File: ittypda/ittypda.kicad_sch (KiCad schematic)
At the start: 149 parts, among them CN1 S2B-PH-SM4-TB, J1 USB_C_Receptacle_USB2.0_14P, J2 Conn_01x04_Pin, SW1 Switch, SW10 Switch, SW11 Switch, SW12 Switch, SW13 Switch, SW14 Switch, SW15 Switch, SW16 Switch, SW17 Switch, SW18 Switch, SW19 Switch, SW2 Switch, SW20 Switch, SW21 Switch, SW22 Switch, SW23 Switch, SW24 Switch, SW25 SLIDE SWITCH, SW26 Switch, SW27 Switch, SW28 Switch, SW29 Switch, SW3 Switch, SW30 Switch, SW31 Switch, SW32 Switch, SW33 Switch, SW34 Switch, SW36 Switch, SW37 Switch, SW38 Switch, SW39 Switch, SW4 Switch, SW41 Switch, SW42 Switch, SW43 Switch, SW44 Switch, SW45 Switch, SW46 Switch, SW47 Switch, SW48 Switch, SW49 Switch, SW5 Switch, SW50 Switch, SW51 Switch, SW52 Switch, SW53 Switch, SW54 Switch, SW55 Switch, SW56 Switch, SW57 Switch, SW58 Switch, SW59 Switch, SW6 Switch, SW60 Switch, SW62 SW_SPDT, SW7 Switch, SW8 Switch, SW9 Switch, U1 STM32F401RETx, U2 BQ24040DSQR, U3 TLV75801PDRV, Y1 16Mhz

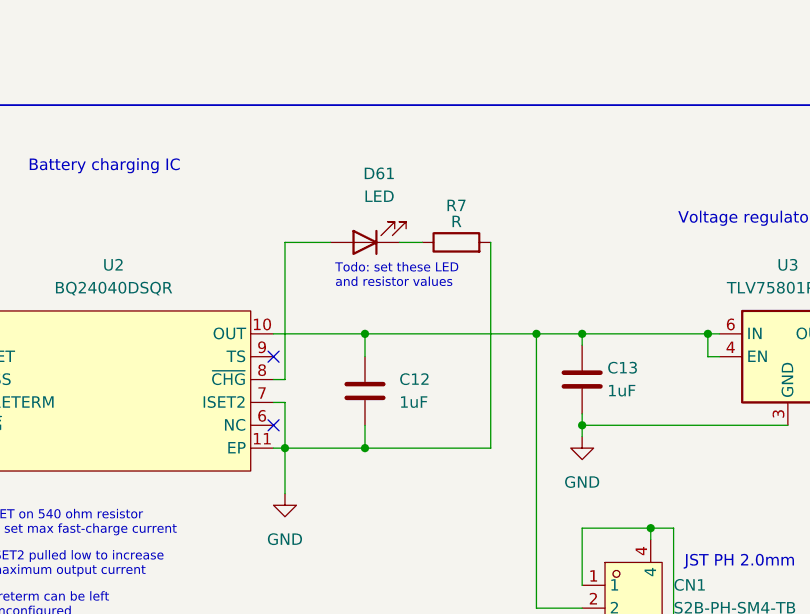
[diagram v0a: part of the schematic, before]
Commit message: add values and footprint for charging status LED
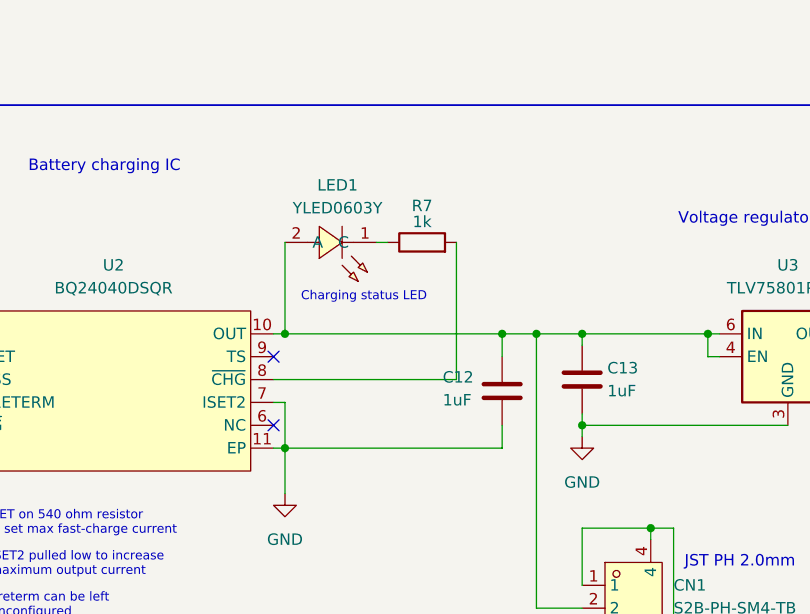
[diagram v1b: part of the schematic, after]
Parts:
- removed D61: LED, symbol Device:LED
- added LED1: YLED0603Y, easyeda2kicad:LED0603-RD-1, symbol easyeda2kicad:YLED0603Y
- R7: value R -> 1k
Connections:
- net GND: no longer R7.2
- net at C12.1, C13.1, CN1.2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: now also LED1.2 (A)
- net at R7.1: now also LED1.1 (C)
- net at U2.8 (~{CHG}): now also R7.2
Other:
- note added: "Charging status LED"
- note removed: "Todo: set these LED and resistor values"
- moved on the sheet: C12, R7
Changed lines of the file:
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@@
 		)
 	)
-	(text "Todo: set these LED\nand resistor values"
+	(text "Charging status LED"
 		(exclude_from_sim no)
-		(at 150.368 171.45 0)
+		(at 146.558 173.736 0)
 		(effects
 			(font
@@
 	)
 	(junction
+		(at 144.78 177.8)
+		(diameter 0)
+		(color 0 0 0 0)
+	)
+	(junction
 		(at 36.83 45.72)
 		(diameter 0)
@@
 	)
 	(junction
-		(at 153.67 177.8)
-		(diameter 0)
-		(color 0 0 0 0)
-	)
-	(junction
 		(at 104.14 118.11)
 		(diameter 0)
@@
 	)
 	(junction
-		(at 153.67 190.5)
-		(diameter 0)
-		(color 0 0 0 0)
-	)
-	(junction
 		(at 209.55 173.99)
 		(diameter 0)
@@
 	)
 	(junction
+		(at 168.91 177.8)
+		(diameter 0)
+		(color 0 0 0 0)
+	)
+	(junction
 		(at 62.23 60.96)
 		(diameter 0)
@@
 	(wire
 		(pts
-			(xy 153.67 177.8) (xy 172.72 177.8)
+			(xy 168.91 177.8) (xy 172.72 177.8)
 		)
 		(stroke
@@
 	(wire
 		(pts
-			(xy 153.67 190.5) (xy 144.78 190.5)
+			(xy 168.91 190.5) (xy 144.78 190.5)
 		)
 		(stroke
@@
 	(wire
 		(pts
+			(xy 144.78 177.8) (xy 168.91 177.8)
+		)
+		(stroke
+			(width 0)
+			(type default)
+		)
+	)
+	(wire
+		(pts
 			(xy 76.2 137.16) (xy 90.17 137.16)
 		)
@@
 	(wire
 		(pts
-			(xy 153.67 187.96) (xy 153.67 190.5)
+			(xy 168.91 187.96) (xy 168.91 190.5)
 		)
 		(stroke
@@
 	(wire
 		(pts
-			(xy 153.67 177.8) (xy 153.67 180.34)
+			(xy 168.91 177.8) (xy 168.91 180.34)
 		)
 		(stroke
@@
 	(wire
 		(pts
-			(xy 144.78 167.64) (xy 149.86 167.64)
-		)
-		(stroke
-			(width 0)
-			(type default)
-		)
-	)
-	(wire
-		(pts
 			(xy 312.42 76.2) (xy 314.96 76.2)
 		)
@@
 	(wire
 		(pts
-			(xy 144.78 182.88) (xy 144.78 167.64)
-		)
-		(stroke
-			(width 0)
-			(type default)
-		)
-	)
-	(wire
-		(pts
 			(xy 62.23 60.96) (xy 76.2 60.96)
 		)
@@
 	(wire
 		(pts
-			(xy 143.51 182.88) (xy 144.78 182.88)
+			(xy 143.51 182.88) (xy 163.83 182.88)
 		)
 		(stroke
@@
 	(wire
 		(pts
-			(xy 157.48 167.64) (xy 160.02 167.64)
+			(xy 154.94 167.64) (xy 156.21 167.64)
 		)
 		(stroke
@@
 	(wire
 		(pts
-			(xy 143.51 177.8) (xy 153.67 177.8)
+			(xy 143.51 177.8) (xy 144.78 177.8)
 		)
 		(stroke
@@
 	(wire
 		(pts
+			(xy 163.83 167.64) (xy 163.83 182.88)
+		)
+		(stroke
+			(width 0)
+			(type default)
+		)
+	)
+	(wire
+		(pts
 			(xy 67.31 177.8) (xy 67.31 176.53)
 		)
@@
 	(wire
 		(pts
-			(xy 153.67 190.5) (xy 167.64 190.5)
-		)
-		(stroke
-			(width 0)
-			(type default)
-		)
-	)
-	(wire
-		(pts
 			(xy 120.65 64.77) (xy 121.92 64.77)
 		)
@@
 	(wire
 		(pts
-			(xy 167.64 190.5) (xy 167.64 167.64)
-		)
-		(stroke
-			(width 0)
-			(type default)
-		)
-	)
-	(wire
-		(pts
 			(xy 64.77 64.77) (xy 64.77 83.82)
 		)
@@
 	(wire
 		(pts
+			(xy 144.78 167.64) (xy 144.78 177.8)
+		)
+		(stroke
+			(width 0)
+			(type default)
+		)
+	)
+	(wire
+		(pts
 			(xy 162.56 83.82) (xy 163.83 83.82)
 		)
@@
 	(symbol
 		(lib_id "Device:R")
-		(at 163.83 167.64 90)
+		(at 160.02 167.64 90)
 		(unit 1)
 		(body_style 1)
@@
 		(dnp no)
 		(property "Reference" "R7"
-			(at 163.83 163.576 90)
+			(at 160.02 163.576 90)
 			(show_name no)
 			(do_not_autoplace no)
@@
 			)
 		)
-		(property "Value" "R"
-			(at 163.83 165.354 90)
+		(property "Value" "1k"
+			(at 160.02 165.354 90)
 			(show_name no)
 			(do_not_autoplace no)
@@
 		)
 		(property "Footprint" ""
-			(at 163.83 169.418 90)
+			(at 160.02 169.418 90)
 			(hide yes)
 			(show_name no)
@@
 		)
 		(property "Datasheet" ""
-			(at 163.83 167.64 0)
+			(at 160.02 167.64 0)
 			(hide yes)
 			(show_name no)
@@
 		)
 		(property "Description" "Resistor"
-			(at 163.83 167.64 0)
+			(at 160.02 167.64 0)
 			(hide yes)
 			(show_name no)
@@
 	)
 	(symbol
-		(lib_id "Device:LED")
-		(at 153.67 167.64 180)
+		(lib_id "power:GND")
+		(at 144.78 195.58 0)
 		(unit 1)
 		(body_style 1)
@@
 		(dnp no)
 		(fields_autoplaced yes)
-		(property "Reference" "D61"
-			(at 155.2575 160.02 0)
+		(property "Reference" "#PWR017"
+			(at 144.78 201.93 0)
+			(hide yes)
 			(show_name no)
 			(do_not_autoplace no)
@@
 			)
 		)
-		(property "Value" "LED"
-			(at 155.2575 162.56 0)
+		(property "Value" "GND"
+			(at 144.78 200.66 0)
 			(show_name no)
 			(do_not_autoplace no)
@@
 		)
 		(property "Footprint" ""
-			(at 153.67 167.64 0)
+			(at 144.78 195.58 0)
 			(hide yes)
 			(show_name no)
@@
 		)
 		(property "Datasheet" ""
-			(at 153.67 167.64 0)
-			(hide yes)
-			(show_name no)
-			(do_not_autoplace no)
-			(effects
-				(font
-					(size 1.27 1.27)
-				)
-			)
-		)
-		(property "Description" "Light emitting diode"
-			(at 153.67 167.64 0)
+			(at 144.78 195.58 0)
 			(hide yes)
 			(show_name no)
@@
 			)
 		)
-		(property "Sim.Pins" "1=K 2=A"
-			(at 153.67 167.64 0)
+		(property "Description" "Power symbol creates a global label with name \"GND\" , ground"
+			(at 144.78 195.58 0)
 			(hide yes)
 			(show_name no)
@@
 			)
 		)
-		(pin "2"
-		)
 		(pin "1"
 		)
@@
 			(project "ittypda"
 				(path "/d1aa8f6c-1644-4347-b86d-2b771500f753"
-					(reference "D61")
+					(reference "#PWR017")
 					(unit 1)
 				)
@@
 	)
 	(symbol
-		(lib_id "power:GND")
-		(at 144.78 195.58 0)
+		(lib_id "easyeda2kicad:YLED0603Y")
+		(at 149.86 168.91 180)
 		(unit 1)
 		(body_style 1)
@@
 		(dnp no)
 		(fields_autoplaced yes)
-		(property "Reference" "#PWR017"
-			(at 144.78 201.93 0)
+		(property "Reference" "LED1"
+			(at 150.62 161.29 0)
+			(show_name no)
+			(do_not_autoplace no)
+			(effects
+				(font
+					(size 1.27 1.27)
+				)
+			)
+		)
+		(property "Value" "YLED0603Y"
+			(at 150.62 163.83 0)
+			(show_name no)
+			(do_not_autoplace no)
+			(effects
+				(font
+					(size 1.27 1.27)
+				)
+			)
+		)
+		(property "Footprint" "easyeda2kicad:LED0603-RD-1"
+			(at 149.86 160.02 0)
 			(hide yes)
 			(show_name no)
@@
 			)
 		)
-		(property "Value" "GND"
-			(at 144.78 200.66 0)
+		(property "Datasheet" "https://www.lcsc.com/datasheet/C19273152.pdf"
+			(at 149.86 157.48 0)
+			(hide yes)
 			(show_name no)
 			(do_not_autoplace no)
@@
 			)
 		)
-		(property "Footprint" ""
-			(at 144.78 195.58 0)
+		(property "Description" ""
+			(at 149.86 168.91 0)
 			(hide yes)
 			(show_name no)
@@
 			)
 		)
-		(property "Datasheet" ""
-			(at 144.78 195.58 0)
+		(property "Manufacturer" "YONGYUTAI(永裕泰)"
+			(at 149.86 154.94 0)
 			(hide yes)
 			(show_name no)
@@
 			)
 		)
-		(property "Description" "Power symbol creates a global label with name \"GND\" , ground"
-			(at 144.78 195.58 0)
+		(property "MPN" "YLED0603Y"
+			(at 149.86 152.4 0)
+			(hide yes)
+			(show_name no)
+			(do_not_autoplace no)
+			(effects
+				(font
+					(size 1.27 1.27)
+				)
+			)
+		)
+		(property "LCSC Part" "C19273152"
+			(at 149.86 149.86 0)
 			(hide yes)
 			(show_name no)
@@
 		(pin "1"
 		)
+		(pin "2"
+		)
 		(instances
 			(project "ittypda"
 				(path "/d1aa8f6c-1644-4347-b86d-2b771500f753"
-					(reference "#PWR017")
+					(reference "LED1")
 					(unit 1)
 				)
@@
 	(symbol
 		(lib_id "Device:C")
-		(at 153.67 184.15 0)
+		(at 168.91 184.15 0)
 		(unit 1)
 		(body_style 1)
@@
 		(in_pos_files yes)
 		(dnp no)
-		(fields_autoplaced yes)
 		(property "Reference" "C12"
-			(at 157.48 182.8799 0)
+			(at 162.306 182.626 0)
 			(show_name no)
 			(do_not_autoplace no)
@@
 		)
 		(property "Value" "1uF"
-			(at 157.48 185.4199 0)
+			(at 162.306 185.166 0)
 			(show_name no)
 			(do_not_autoplace no)
@@
 		)
 		(property "Footprint" ""
-			(at 154.6352 187.96 0)
+			(at 169.8752 187.96 0)
 			(hide yes)
 			(show_name no)
@@
 		)
 		(property "Datasheet" ""
-			(at 153.67 184.15 0)
+			(at 168.91 184.15 0)
 			(hide yes)
 			(show_name no)
@@
 		)
 		(property "Description" "Unpolarized capacitor"
-			(at 153.67 184.15 0)
+			(at 168.91 184.15 0)
 			(hide yes)
 			(show_name no)

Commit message: add todo
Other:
- note added: "Todo: check whether states should be inverted based on vibes"
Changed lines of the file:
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@@
+		)
+	)
+	(text "Todo: check whether\nstates should be\ninverted based on\nvibes"
+		(exclude_from_sim no)
+		(at 201.168 158.242 0)
+		(effects
+			(font
+				(size 1 1)
+			)
+			(justify left)
 		)
 	)

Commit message: assign footprints!!
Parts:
- removed SW62: SW_SPDT, symbol Switch:SW_SPDT
- added SW61: Switch, easyeda2kicad:SW-SMD_4P-L5.1-W5.1-P3.70-LS6.5-TL_H1.5, symbol easyeda2kicad:TS-1187A-B-A-B
- C1, C10, C11, C12, C13, C14, C15, C2, C3, C4, C5, C6, C7, C8, C9: footprint (none) -> Capacitor_SMD:C_0402_1005Metric
- J1: footprint (none) -> Connector_USB:USB_C_Receptacle_HRO_TYPE-C-31-M-12
- R1, R2, R3, R4, R5, R6, R7, R8, R9: footprint (none) -> Resistor_SMD:R_0402_1005Metric
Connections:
- net +3.3V: now also SW61.4 (D)
- net GND: now also R1.1
- net at R1.2, U1.60 (BOOT0): now also SW61.2 (B)
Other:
- moved on the sheet: R1

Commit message: add 3d model for usb c port and finalize initial placement of parts (not diodes yet)
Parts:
- J1: footprint Connector_USB:USB_C_Receptacle_HRO_TYPE-C-31-M-12 -> easyeda2kicad:USB-C_SMD-TYPE-C-31-M-12_1; LCSC Part (none) -> C165948
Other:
- moved on the sheet: C12
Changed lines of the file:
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@@
 	)
 	(junction
-		(at 106.68 45.72)
+		(at 157.48 177.8)
 		(diameter 0)
 		(color 0 0 0 0)
 	)
 	(junction
-		(at 176.53 102.87)
+		(at 106.68 45.72)
 		(diameter 0)
 		(color 0 0 0 0)
 	)
 	(junction
-		(at 191.77 177.8)
+		(at 176.53 102.87)
 		(diameter 0)
 		(color 0 0 0 0)
 	)
 	(junction
-		(at 306.07 41.91)
+		(at 191.77 177.8)
 		(diameter 0)
 		(color 0 0 0 0)
 	)
 	(junction
-		(at 168.91 177.8)
+		(at 306.07 41.91)
 		(diameter 0)
 		(color 0 0 0 0)
@@
 	(wire
 		(pts
-			(xy 168.91 177.8) (xy 172.72 177.8)
-		)
-		(stroke
-			(width 0)
-			(type default)
-		)
-	)
-	(wire
-		(pts
 			(xy 64.77 39.37) (xy 64.77 45.72)
 		)
@@
 	(wire
 		(pts
-			(xy 168.91 190.5) (xy 144.78 190.5)
+			(xy 157.48 190.5) (xy 144.78 190.5)
 		)
 		(stroke
@@
 	(wire
 		(pts
-			(xy 144.78 177.8) (xy 168.91 177.8)
+			(xy 144.78 177.8) (xy 157.48 177.8)
 		)
 		(stroke
@@
 	(wire
 		(pts
-			(xy 168.91 187.96) (xy 168.91 190.5)
+			(xy 157.48 193.04) (xy 157.48 190.5)
 		)
 		(stroke
@@
 	(wire
 		(pts
-			(xy 168.91 177.8) (xy 168.91 180.34)
+			(xy 157.48 177.8) (xy 157.48 185.42)
 		)
 		(stroke
@@
 	(wire
 		(pts
+			(xy 157.48 177.8) (xy 172.72 177.8)
+		)
+		(stroke
+			(width 0)
+			(type default)
+		)
+	)
+	(wire
+		(pts
 			(xy 92.71 102.87) (xy 93.98 102.87)
 		)
@@
 			)
 		)
-		(property "Footprint" "Connector_USB:USB_C_Receptacle_HRO_TYPE-C-31-M-12"
+		(property "Footprint" "easyeda2kicad:USB-C_SMD-TYPE-C-31-M-12_1"
 			(at 38.1 184.15 0)
 			(hide yes)
@@
 			)
 		)
+		(property "LCSC Part" "C165948"
+			(at 34.29 184.15 0)
+			(hide yes)
+			(show_name no)
+			(do_not_autoplace no)
+			(effects
+				(font
+					(size 1.27 1.27)
+				)
+			)
+		)
 		(pin "B6"
 		)
@@
 	(symbol
 		(lib_id "Device:C")
-		(at 168.91 184.15 0)
+		(at 157.48 189.23 0)
 		(unit 1)
 		(body_style 1)
@@
 		(dnp no)
 		(property "Reference" "C12"
-			(at 162.306 182.626 0)
+			(at 150.876 187.706 0)
 			(show_name no)
 			(do_not_autoplace no)
@@
 		)
 		(property "Value" "1uF"
-			(at 162.306 185.166 0)
+			(at 150.876 190.246 0)
 			(show_name no)
 			(do_not_autoplace no)
@@
 		)
 		(property "Footprint" "Capacitor_SMD:C_0402_1005Metric"
-			(at 169.8752 187.96 0)
+			(at 158.4452 193.04 0)
 			(hide yes)
 			(show_name no)
@@
 		)
 		(property "Datasheet" ""
-			(at 168.91 184.15 0)
+			(at 157.48 189.23 0)
 			(hide yes)
 			(show_name no)
@@
 		)
 		(property "Description" "Unpolarized capacitor"
-			(at 168.91 184.15 0)
+			(at 157.48 189.23 0)
 			(hide yes)
 			(show_name no)

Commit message: split power circuitry into seperate PCB part
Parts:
- added J10, J4: Solder Pad D+, TestPoint:TestPoint_Pad_D1.5mm, symbol Connector:Conn_01x01_Pin
- added J11, J12: Solder Pad GND, TestPoint:TestPoint_Pad_D1.5mm, symbol Connector:Conn_01x01_Pin
- added J3, J9: Solder Pad D-, TestPoint:TestPoint_Pad_D1.5mm, symbol Connector:Conn_01x01_Pin
- added J5, J8: Solder Pad 3.3V, TestPoint:TestPoint_Pad_D1.5mm, symbol Connector:Conn_01x01_Pin
- added J6, J7: Solder Pad VBAT, TestPoint:TestPoint_Pad_D1.5mm, symbol Connector:Conn_01x01_Pin
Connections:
- net +3.3V: now also J8.1 (Pin_1); no longer SW25.3
- net GND: now also J11.1 (Pin_1), J12.1 (Pin_1)
- net USB_D+: no longer names the net of J1.A6 (D+), J1.B6 (D+)
- net USB_D+: now also J4.1 (Pin_1); no longer R5.2
- net USB_D-: no longer names the net of J1.A7 (D-), J1.B7 (D-)
- net USB_D-: now also J3.1 (Pin_1); no longer R4.2
- net VBAT: no longer names the net of C14.1, R8.1, SW25.2, U3.1 (OUT)
- net VBAT: now also J6.1 (Pin_1); no longer U1.1 (VBAT)
- new net: J10.1 (Pin_1), R5.2
- new net: J9.1 (Pin_1), R4.2
- new net: J5.1 (Pin_1), SW25.3
- new net: J7.1 (Pin_1), U1.1 (VBAT)

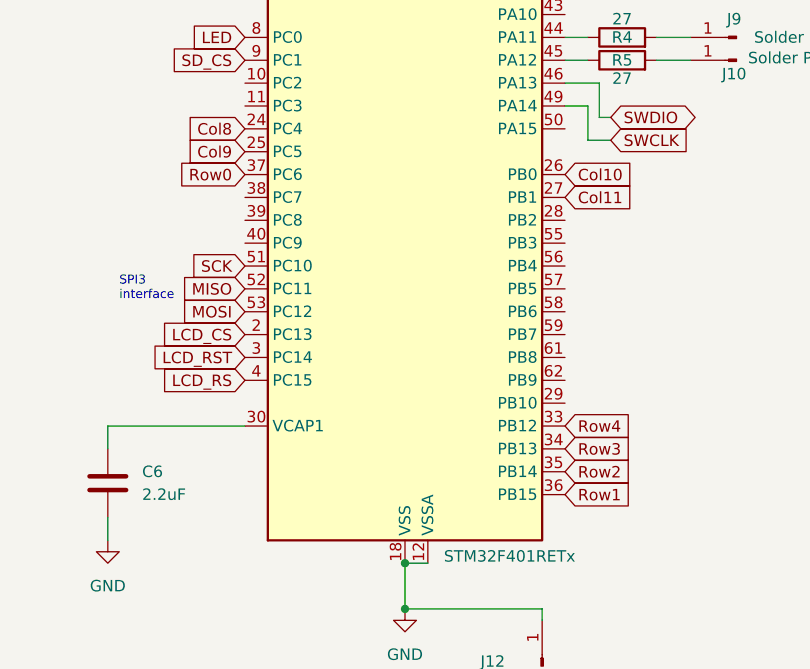
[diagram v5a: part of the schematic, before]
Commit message: connect rows of keyboard matrix to microcontroller
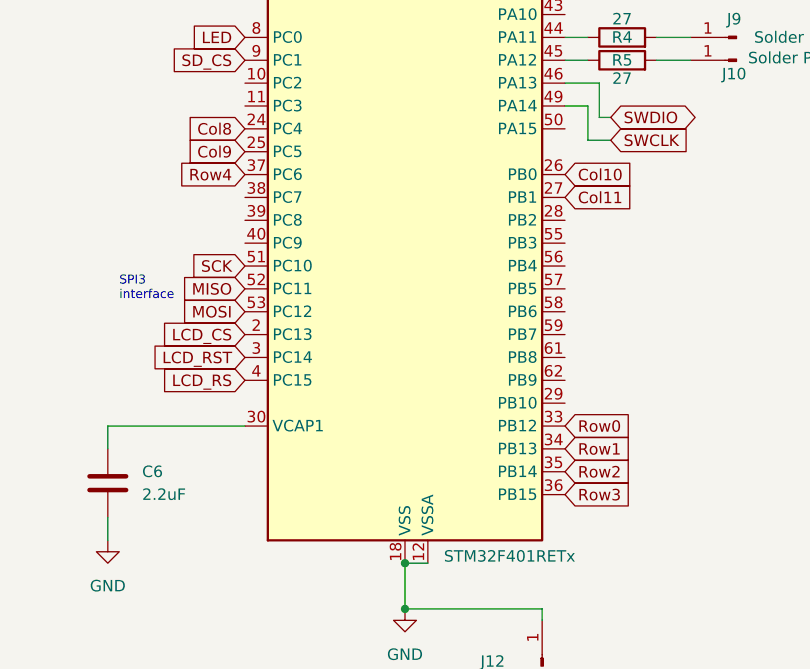
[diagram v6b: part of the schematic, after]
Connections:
- net Row0: now also U1.33 (PB12); no longer U1.37 (PC6)
- net Row1: now also U1.34 (PB13); no longer U1.36 (PB15)
- net Row3: now also U1.36 (PB15); no longer U1.34 (PB13)
- net Row4: now also U1.37 (PC6); no longer U1.33 (PB12)

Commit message: change connector type between the two pcbs and wire it up on the mainboard
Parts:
- removed J10, J4: Solder Pad D+, TestPoint:TestPoint_Pad_D1.5mm, symbol Connector:Conn_01x01_Pin
- removed J11, J12: Solder Pad GND, TestPoint:TestPoint_Pad_D1.5mm, symbol Connector:Conn_01x01_Pin
- removed J3, J9: Solder Pad D-, TestPoint:TestPoint_Pad_D1.5mm, symbol Connector:Conn_01x01_Pin
- removed J5, J8: Solder Pad 3.3V, TestPoint:TestPoint_Pad_D1.5mm, symbol Connector:Conn_01x01_Pin
- removed J6, J7: Solder Pad VBAT, TestPoint:TestPoint_Pad_D1.5mm, symbol Connector:Conn_01x01_Pin
- added J13, J14: Conn_01x05_Pin, Connector_PinHeader_2.54mm:PinHeader_1x05_P2.54mm_Vertical, symbol Connector:Conn_01x05_Pin
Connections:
- net +3.3V: now also J2.1 (Pin_1), J14.2 (Pin_2)
- net GND: now also J2.3 (Pin_3), J13.1 (Pin_1), J14.1 (Pin_1)
- net SWCLK: now also J2.2 (Pin_2)
- net SWDIO: now also J2.4 (Pin_4)
- net InD-: now reaches R5.2
- net InD-: now also J14.5 (Pin_5)
- net OutD+: now reaches J1.A7 (D-), J1.B7 (D-)
- net OutD+: now also J13.4 (Pin_4)
- net OutVBAT: now reaches C14.1, R8.1, SW25.2, U3.1 (OUT)
- net OutVBAT: now also J13.3 (Pin_3)
- net OutD-: now reaches J1.A6 (D+), J1.B6 (D+)
- net OutD-: now also J13.5 (Pin_5)
- net InD+: now reaches R4.2
- net InD+: now also J14.4 (Pin_4)
- net Out3V3: now reaches SW25.3
- net Out3V3: now also J13.2 (Pin_2)
- net InVBAT: now reaches U1.1 (VBAT)
- net InVBAT: now also J14.3 (Pin_3)
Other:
- moved on the sheet: FPC1, J2
